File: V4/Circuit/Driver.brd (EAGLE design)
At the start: 58.1 x 81.3 mm, 54 parts, among them IC1 DRV8303DCA

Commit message: Ready for V4 autoroutering 7
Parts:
- moved AVDD_CAP 0.79 mm to (42.1, 55.6)
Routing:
- net SO1B: track 15.2 -> 11.3 mm
- net GND: track 335.0 -> 334.3 mm
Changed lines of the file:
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@@
 <attribute name="VALUE" x="44.45" y="42.3545" size="0.6096" layer="28" font="vector" ratio="20" rot="MR180" align="top-center"/>
 </element>
-<element name="AVDD_CAP" library="SparkFun-Capacitors" package="0603" value="1.0uF" x="41.275" y="55.5625" smashed="yes" rot="MR180">
-<attribute name="NAME" x="41.275" y="54.8005" size="0.6096" layer="26" font="vector" ratio="20" rot="MR180" align="bottom-center"/>
-<attribute name="PROD_ID" value="CAP-00868" x="41.275" y="55.5625" size="1.778" layer="28" rot="MR180" display="off"/>
-<attribute name="VALUE" x="41.275" y="56.3245" size="0.6096" layer="28" font="vector" ratio="20" rot="MR180" align="top-center"/>
+<element name="AVDD_CAP" library="SparkFun-Capacitors" package="0603" value="1.0uF" x="42.06875" y="55.5625" smashed="yes" rot="MR180">
+<attribute name="NAME" x="42.06875" y="54.8005" size="0.6096" layer="26" font="vector" ratio="20" rot="MR180" align="bottom-center"/>
+<attribute name="PROD_ID" value="CAP-00868" x="42.06875" y="55.5625" size="1.778" layer="28" rot="MR180" display="off"/>
+<attribute name="VALUE" x="42.06875" y="56.3245" size="0.6096" layer="28" font="vector" ratio="20" rot="MR180" align="top-center"/>
 </element>
 <element name="R2" library="SparkFun-Resistors" package="0603" value="10k" x="24.765" y="53.34" smashed="yes" rot="MR270">
@@
 <wire x1="30.241875" y1="56.276875" x2="29.21" y2="55.245" width="1.016" layer="16"/>
 <wire x1="29.21" y1="55.245" x2="29.21" y2="54.61" width="1.016" layer="16"/>
-<wire x1="38.4581" y1="50.5231" x2="35.2425" y2="47.3075" width="1.27" layer="16"/>
-<wire x1="41.28615" y1="50.5231" x2="38.4581" y2="50.5231" width="1.27" layer="16"/>
-<wire x1="42.125" y1="51.36195" x2="42.125" y2="55.5625" width="1.27" layer="16"/>
-<wire x1="42.125" y1="51.36195" x2="41.28615" y2="50.5231" width="1.27" layer="16"/>
-<wire x1="35.2425" y1="47.3075" x2="35.2425" y2="47.9425" width="1.27" layer="16"/>
-<wire x1="35.2425" y1="47.9425" x2="35.56" y2="48.26" width="1.27" layer="16"/>
 <wire x1="29.21" y1="16.77" x2="29.21" y2="15.24" width="0.381" layer="16"/>
 <wire x1="29.21" y1="15.24" x2="29.21" y2="13.97" width="0.381" layer="16"/>
@@
 <wire x1="40.50394375" y1="48.26" x2="44.8104" y2="43.95354375" width="1.016" layer="16"/>
 <wire x1="45.3" y1="43.18" x2="45.3" y2="41.5925" width="1.016" layer="16"/>
-<wire x1="41.7624" y1="56.38865" x2="41.7624" y2="55.9251" width="1.27" layer="16"/>
-<wire x1="41.7624" y1="55.9251" x2="42.125" y2="55.5625" width="1.27" layer="16"/>
-<wire x1="37.759375" y1="57.30875" x2="40.8423" y2="57.30875" width="1.27" layer="16"/>
-<wire x1="40.8423" y1="57.30875" x2="41.7624" y2="56.38865" width="1.27" layer="16"/>
+<wire x1="42.55615" y1="56.38865" x2="42.55615" y2="55.9251" width="1.27" layer="16"/>
+<wire x1="42.55615" y1="55.9251" x2="42.91875" y2="55.5625" width="1.27" layer="16"/>
+<wire x1="37.759375" y1="57.30875" x2="41.63605" y2="57.30875" width="1.27" layer="16"/>
+<wire x1="41.63605" y1="57.30875" x2="42.55615" y2="56.38865" width="1.27" layer="16"/>
+<wire x1="41.795" y1="52.522475" x2="41.795" y2="52.048" width="1.27" layer="16"/>
+<wire x1="42.91875" y1="55.5625" x2="42.91875" y2="53.646225" width="1.27" layer="16"/>
+<wire x1="42.91875" y1="53.646225" x2="41.795" y2="52.522475" width="1.27" layer="16"/>
+<wire x1="41.795" y1="52.048" x2="41.795" y2="51.03195" width="1.27" layer="16"/>
+<wire x1="41.795" y1="51.03195" x2="39.02305" y2="48.26" width="1.27" layer="16"/>
+<wire x1="39.02305" y1="48.26" x2="35.56" y2="48.26" width="1.27" layer="16"/>
+<wire x1="42.91875" y1="55.5625" x2="50.165" y2="61.9125" width="0" layer="19" extent="16-16"/>
+<wire x1="32.2825" y1="56.276875" x2="30.5825" y2="56.276875" width="0" layer="19" extent="1-16"/>
+<wire x1="3.568" y1="55.245" x2="9.31" y2="39.37" width="0" layer="19" extent="1-1"/>
+<wire x1="4.445" y1="77.1525" x2="3.568" y2="55.245" width="0" layer="19" extent="1-1"/>
+<wire x1="6.985" y1="77.1525" x2="4.445" y2="77.1525" width="0" layer="19" extent="1-1"/>
 </signal>
 <signal name="N$4">
@@
 <contactref element="DVDD_CAP" pad="1"/>
 <contactref element="DVDD" pad="TP"/>
-<wire x1="38.81" y1="52.9475" x2="38.81" y2="52.048" width="0.3048" layer="16"/>
-<wire x1="37.465" y1="54.2925" x2="38.81" y2="52.9475" width="0.381" layer="16"/>
-<wire x1="36.059375" y1="57.30875" x2="37.465" y2="55.903125" width="0.508" layer="16"/>
-<wire x1="37.465" y1="55.903125" x2="37.465" y2="54.2925" width="0.508" layer="16"/>
+<wire x1="36.059375" y1="57.30875" x2="36.059375" y2="56.015625" width="0.508" layer="16"/>
+<wire x1="36.059375" y1="56.015625" x2="36.195" y2="55.88" width="0.508" layer="16"/>
+<wire x1="36.195" y1="55.88" x2="37.7825" y2="54.2925" width="0.508" layer="16"/>
+<wire x1="37.7825" y1="54.2925" x2="38.8029" y2="53.2721" width="0.381" layer="16"/>
+<wire x1="38.8029" y1="53.2721" x2="38.8029" y2="52.705" width="0.381" layer="16"/>
+<wire x1="38.8029" y1="52.705" x2="38.8029" y2="52.0551" width="0.3048" layer="16"/>
+<wire x1="38.8029" y1="52.0551" x2="38.81" y2="52.048" width="0.3048" layer="16"/>
 <wire x1="38.81" y1="52.048" x2="53.81625" y2="49.2125" width="0" layer="19" extent="1-16"/>
 </signal>
@@
 <contactref element="IC1" pad="23"/>
 <contactref element="AVDD_CAP" pad="1"/>
-<wire x1="40.425" y1="55.5625" x2="40.425" y2="54.4524" width="0.508" layer="16"/>
-<wire x1="40.425" y1="54.4524" x2="40.8434" y2="54.034" width="0.508" layer="16"/>
-<wire x1="40.8434" y1="54.034" x2="40.8434" y2="53.0436375" width="0.508" layer="16"/>
+<wire x1="41.21875" y1="55.5625" x2="40.8434" y2="55.18715" width="0.508" layer="16"/>
+<wire x1="40.8434" y1="55.18715" x2="40.8434" y2="53.0436375" width="0.508" layer="16"/>
 <wire x1="40.8434" y1="53.0436375" x2="40.8434" y2="52.95383125" width="0.381" layer="16"/>
 <wire x1="40.8434" y1="52.95383125" x2="40.8171" y2="52.92753125" width="0.381" layer="16"/>
@@
 <contactref element="IC1" pad="21"/>
 <contactref element="R5" pad="2"/>
-<via x="38.84238125" y="55.800625" extent="1-16" drill="0.35"/>
-<wire x1="38.84238125" y1="54.3069375" x2="38.84238125" y2="55.800625" width="0.254" layer="16"/>
-<wire x1="39.7498" y1="53.39951875" x2="38.84238125" y2="54.3069375" width="0.254" layer="16"/>
-<wire x1="39.81" y1="52.048" x2="39.7498" y2="52.1082" width="0.254" layer="16"/>
-<wire x1="39.7498" y1="52.1082" x2="39.7498" y2="53.39951875" width="0.254" layer="16"/>
-<wire x1="47.625" y1="53.76" x2="44.1406" y2="53.76" width="0.254" layer="16"/>
-<wire x1="44.1406" y1="53.76" x2="43.2906" y2="54.61" width="0.254" layer="16"/>
-<via x="43.2906" y="54.61" extent="1-16" drill="0.35"/>
-<wire x1="39.78544375" y1="53.9524" x2="39.24066875" y2="53.9524" width="0.254" layer="1"/>
-<wire x1="39.24066875" y1="53.9524" x2="38.85545625" y2="54.3376125" width="0.254" layer="1"/>
-<wire x1="43.2906" y1="54.61" x2="40.44304375" y2="54.61" width="0.254" layer="1"/>
-<wire x1="38.85545625" y1="54.3376125" x2="38.85545625" y2="55.78755" width="0.254" layer="1"/>
-<wire x1="38.85545625" y1="55.78755" x2="38.84238125" y2="55.800625" width="0.254" layer="1"/>
-<wire x1="40.44304375" y1="54.61" x2="39.78544375" y2="53.9524" width="0.254" layer="1"/>
+<via x="39.47738125" y="54.689375" extent="1-16" drill="0.35"/>
+<via x="44.2431" y="54.61" extent="1-16" drill="0.35"/>
+<wire x1="39.81" y1="52.048" x2="39.81" y2="54.35675625" width="0.3048" layer="16"/>
+<wire x1="39.81" y1="54.35675625" x2="39.47738125" y2="54.689375" width="0.3048" layer="16"/>
+<wire x1="39.55675625" y1="54.61" x2="39.47738125" y2="54.689375" width="0.3048" layer="1"/>
+<wire x1="39.55675625" y1="54.61" x2="44.2431" y2="54.61" width="0.3048" layer="1"/>
+<wire x1="47.625" y1="53.76" x2="45.0931" y2="53.76" width="0.3048" layer="16"/>
+<wire x1="45.0931" y1="53.76" x2="44.2431" y2="54.61" width="0.3048" layer="16"/>
 </signal>
 <signal name="SO2B">
 <contactref element="IC1" pad="22"/>
 <contactref element="R6" pad="2"/>
-<wire x1="40.31" y1="52.048" x2="40.31" y2="53.81305625" width="0.254" layer="16"/>
-<wire x1="40.31" y1="53.81305625" x2="39.51305625" y2="54.61" width="0.254" layer="16"/>
-<via x="39.51305625" y="54.61" extent="1-16" drill="0.35"/>
-<wire x1="39.51305625" y1="54.61" x2="40.46555625" y2="55.5625" width="0.254" layer="1"/>
-<wire x1="40.46555625" y1="55.5625" x2="43.2906" y2="55.5625" width="0.254" layer="1"/>
-<via x="43.2906" y="55.5625" extent="1-16" drill="0.35"/>
-<wire x1="43.2906" y1="55.5625" x2="46.07736875" y2="55.5625" width="0.254" layer="16"/>
+<via x="39.83055625" y="55.5625" extent="1-16" drill="0.35"/>
+<wire x1="39.83055625" y1="55.5625" x2="44.2431" y2="55.5625" width="0.254" layer="1"/>
+<via x="44.2431" y="55.5625" extent="1-16" drill="0.35"/>
+<wire x1="44.2431" y1="55.5625" x2="46.07736875" y2="55.5625" width="0.254" layer="16"/>
 <wire x1="48.9769" y1="54.6306" x2="49.8475" y2="53.76" width="0.254" layer="16"/>
 <wire x1="46.07736875" y1="55.5625" x2="47.00926875" y2="54.6306" width="0.254" layer="16"/>
 <wire x1="47.00926875" y1="54.6306" x2="48.9769" y2="54.6306" width="0.254" layer="16"/>
+<wire x1="40.31" y1="52.048" x2="40.31" y2="52.78676875" width="0.3048" layer="16"/>
+<wire x1="40.31" y1="52.78676875" x2="40.2846" y2="52.81216875" width="0.3048" layer="16"/>
+<wire x1="40.2846" y1="52.81216875" x2="40.2846" y2="55.10845625" width="0.3048" layer="16"/>
+<wire x1="40.2846" y1="55.10845625" x2="39.83055625" y2="55.5625" width="0.3048" layer="16"/>
 </signal>
 </signals>

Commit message: Ready for V4 autoroutering 8
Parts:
- moved DTC 0.64 mm to (31.4, 56.9)
- moved DVDD_CAP 0.64 mm to (37.5, 57.3)
- moved GVDD_CAP 0.64 mm to (31.4, 56.9)
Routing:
- net GND: track 334.3 -> 333.1 mm
- net GVDD: track 5.05 -> 5.81 mm

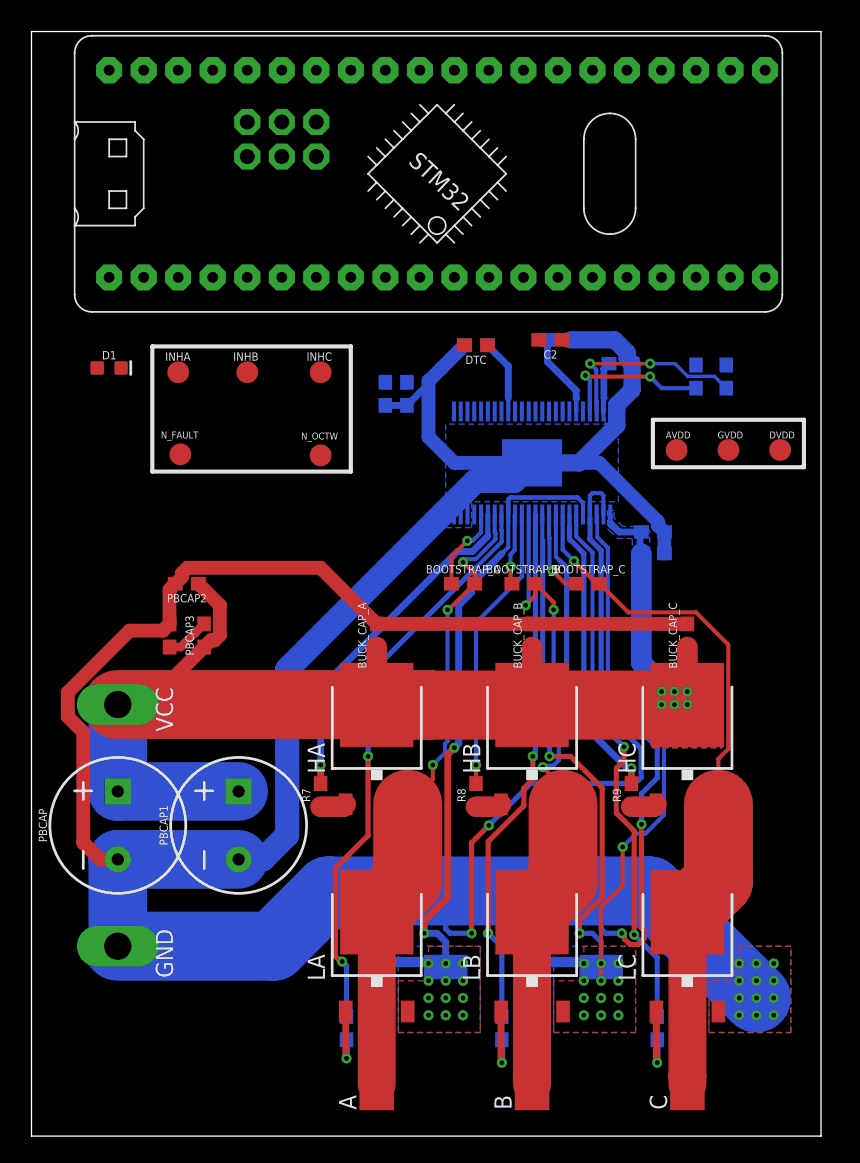
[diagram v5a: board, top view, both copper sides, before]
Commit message: Finished autoRouter
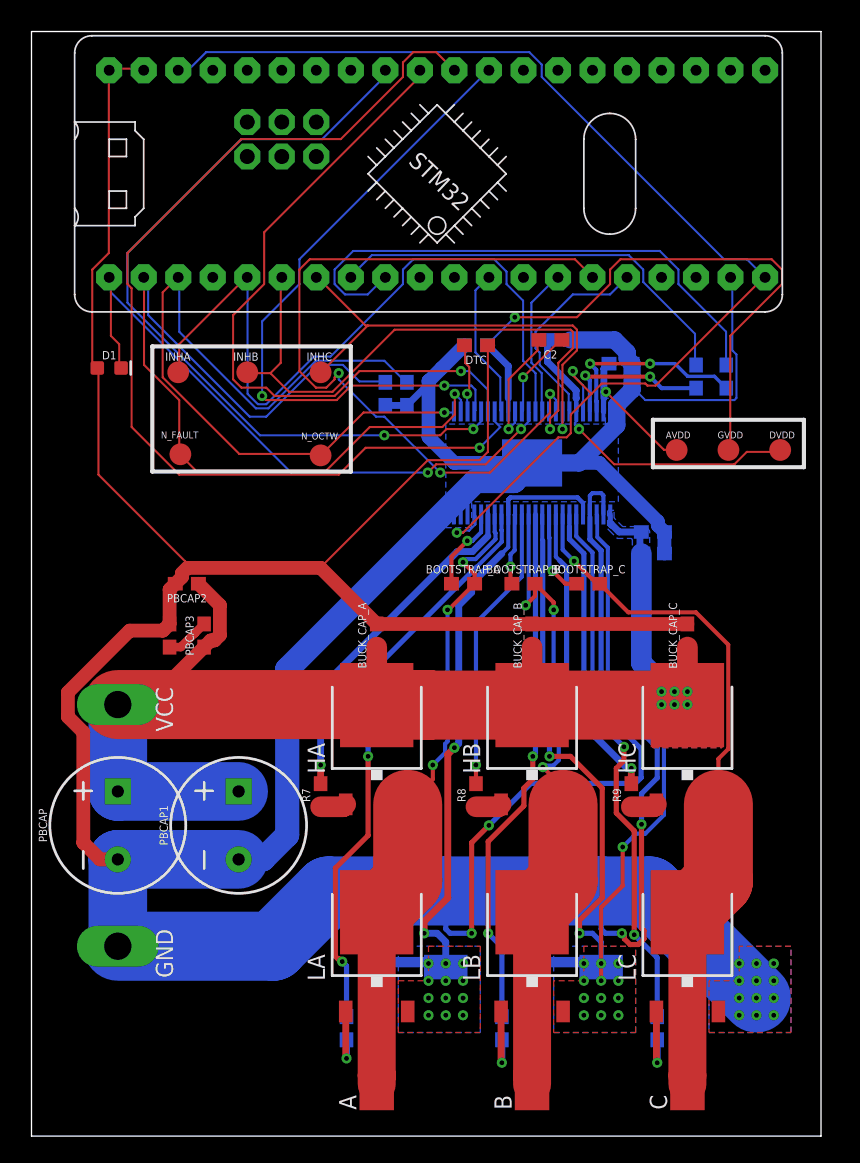
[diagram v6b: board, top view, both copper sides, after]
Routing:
- net 3V3: track 0.00 -> 90.4 mm, vias 0 -> 2
- net GND: track 333.1 -> 416.5 mm
- net SCLK: track 0.00 -> 75.7 mm, vias 0 -> 1
- net N_FAULT: track 0.21 -> 65.5 mm, vias 0 -> 1
- net SDI: track 0.00 -> 59.7 mm, vias 0 -> 2
- net N_OCTW: track 0.00 -> 58.2 mm, vias 0 -> 1
- net INLB: track 0.00 -> 57.4 mm, vias 0 -> 3
- net INHA: track 0.00 -> 53.7 mm
- net SDO: track 0.00 -> 50.6 mm, vias 0 -> 1
- net NSCS: track 0.00 -> 48.9 mm, vias 0 -> 2
- net EN_GATE: track 0.00 -> 46.9 mm, vias 0 -> 2
- net INHB: track 0.00 -> 43.1 mm, vias 0 -> 1
- net SO2: track 0.32 -> 40.9 mm
- net GVDD: track 5.81 -> 46.0 mm, vias 0 -> 1
- net INHC: track 0.00 -> 34.8 mm, vias 0 -> 1
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
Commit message: Exported V4 circuit
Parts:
- added ENCODER: (no value), con-lstb:MA06-1
- added SERIAL: (no value), con-lstb:MA04-1
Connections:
- removed net PA0: U$1.P$36
- removed net PA1: U$1.P$35
- new net PA11: ENCODER.6, U$1.P$8
- new net PA12: ENCODER.5, U$1.P$9
- net 3V3: now also ENCODER.1, SERIAL.1
- net GND: now also ENCODER.2, ENCODER.3, SERIAL.2
- net PA15: now also ENCODER.4
- net PA2: now also SERIAL.3
- net PA3: now also SERIAL.4
- net SO1: now also U$1.P$35; no longer U$1.P$8
- net SO2: now also U$1.P$36; no longer U$1.P$9
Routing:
- net 3V3: track 90.4 -> 169.2 mm, vias 2 -> 4
- net GND: track 416.5 -> 494.2 mm, vias 16 -> 23
- net PA3: track 0.00 -> 61.2 mm, vias 0 -> 2
- net PA2: track 0.00 -> 61.0 mm, vias 0 -> 1
- net PA15: track 0.00 -> 58.7 mm, vias 0 -> 2
- net PA12: track 0.00 -> 54.1 mm, vias 0 -> 2
- net PA11: track 0.00 -> 53.1 mm, vias 0 -> 1
- net SO2: track 40.9 -> 24.8 mm, vias 0 -> 1
- net INHC: track 34.8 -> 44.7 mm
- net SO1: track 31.3 -> 24.9 mm, vias 0 -> 1
- net DVDD: track 24.7 -> 24.0 mm
- net SH_C: track 51.3 -> 50.6 mm
- net SH_A: track 46.9 -> 46.3 mm
- net SH_B: track 48.6 -> 48.0 mm
- net GH_C: track 22.3 -> 22.9 mm
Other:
- board size 58.1 x 81.3 mm -> 59 x 81 mm
- board text added: "3V3"
- board text added: "A"
- board text added: "B"
- board text added: "GND"
- board text added: "I"
- board text added: "Rx"
- board text added: "Tx"
